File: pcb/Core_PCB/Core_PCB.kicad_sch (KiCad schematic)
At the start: 0 parts

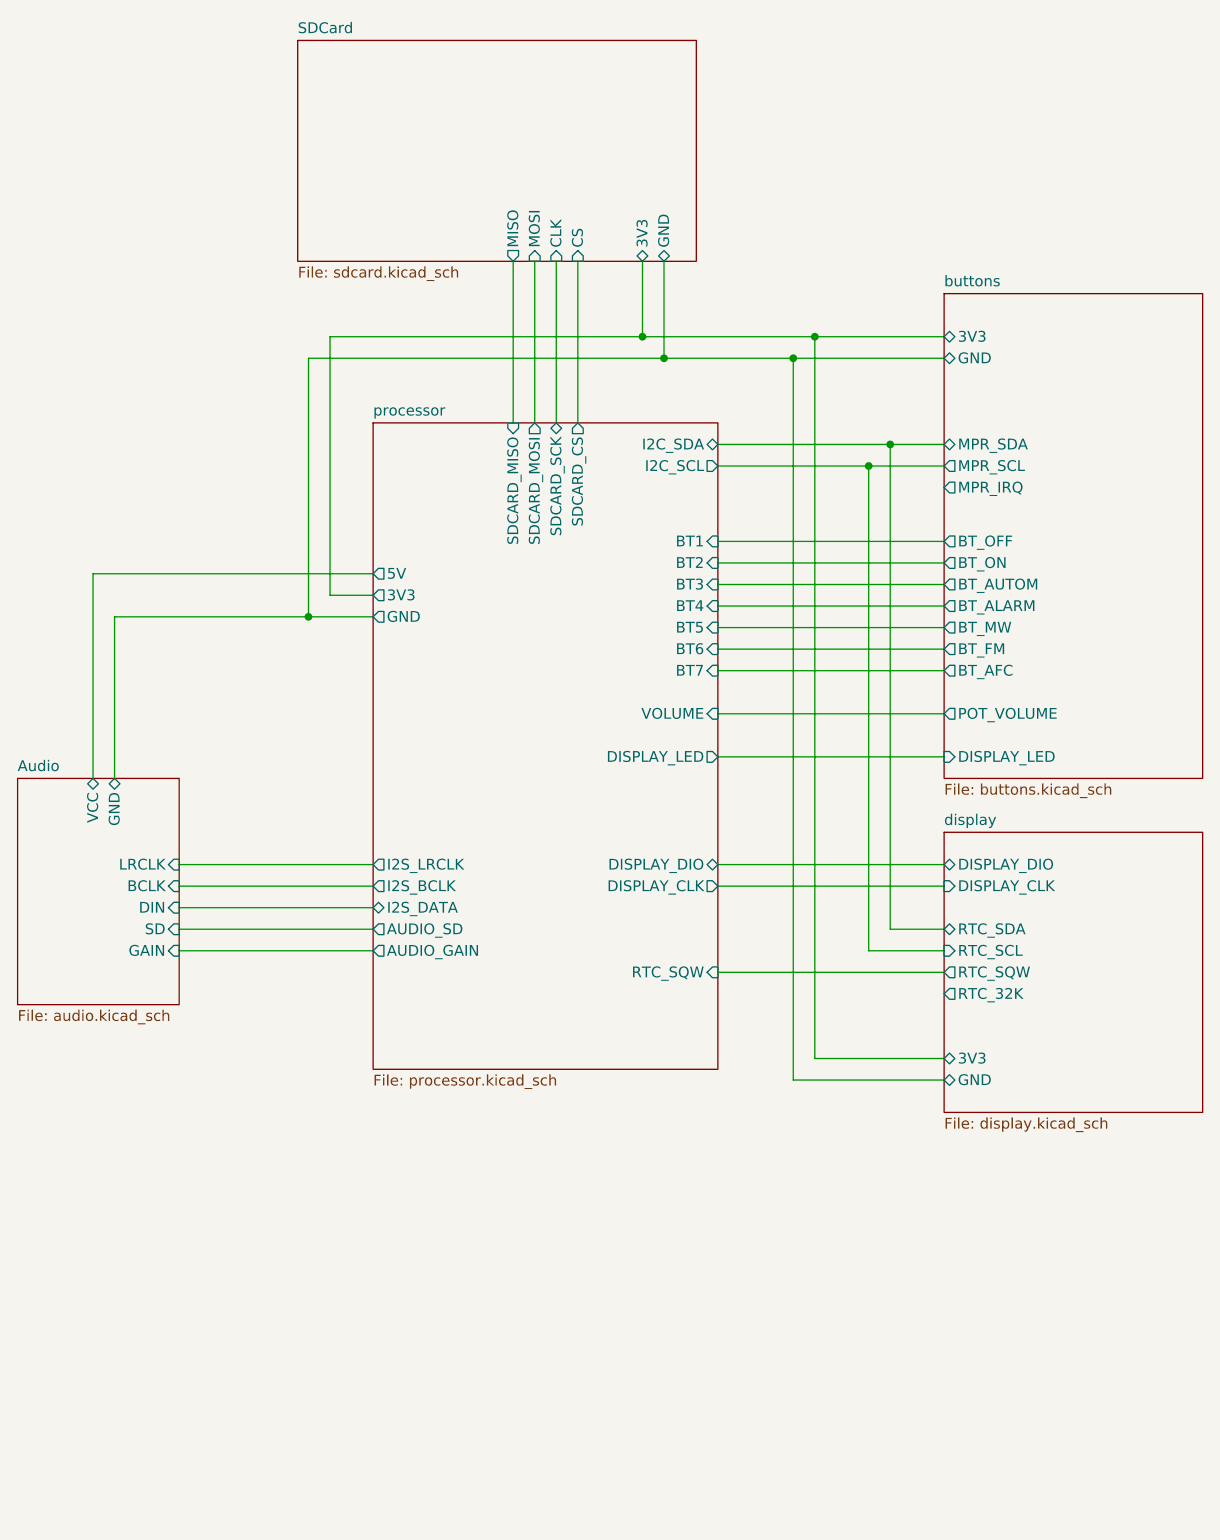
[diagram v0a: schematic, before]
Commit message: SCH: audio gain control via mux (HEF4051), buttons read via i2c io expander (MCP23017)
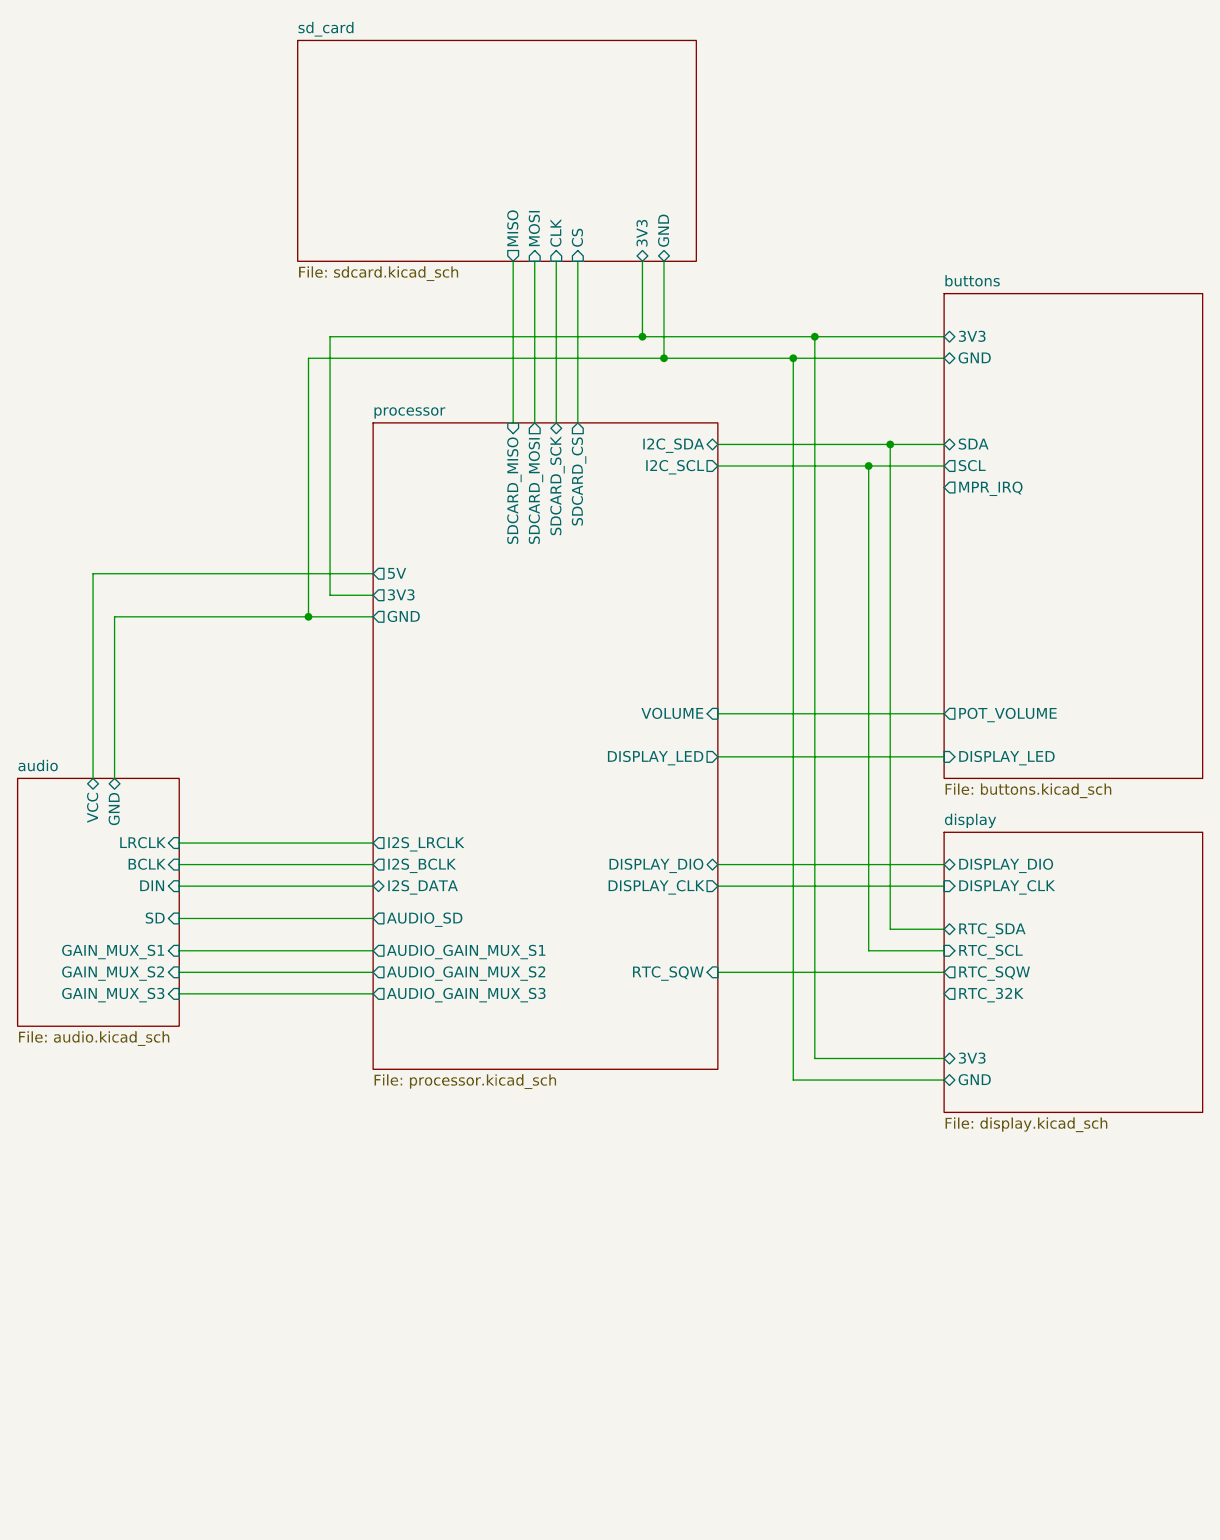
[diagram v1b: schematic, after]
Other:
- sheet Audio renamed audio
- sheet SDCard renamed sd_card
- sheet audio ports: added GAIN_MUX_S1, GAIN_MUX_S2, GAIN_MUX_S3; removed GAIN
- sheet buttons ports: added SCL, SDA; removed BT_AFC, BT_ALARM, BT_AUTOM, BT_FM, BT_MW, BT_OFF, BT_ON, MPR_SCL, MPR_SDA
- sheet processor ports: added AUDIO_GAIN_MUX_S1, AUDIO_GAIN_MUX_S2, AUDIO_GAIN_MUX_S3; removed AUDIO_GAIN, BT1, BT2, BT3, BT4, BT5, BT6, BT7

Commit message: SCH: annotated sheets, reannotated all components
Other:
- company: (none) -> brunolalb@gmail.com
- title: (none) -> Alarm Clock Resto Mod - Core PCB
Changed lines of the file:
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@@
 	(generator_version "10.0")
 	(paper "A4")
+	(title_block
+		(title "Alarm Clock Resto Mod - Core PCB")
+		(date "2026-07-08")
+		(rev "1.0")
+		(company "brunolalb@gmail.com")
+		(comment 1 "Bruno Landau Albrecht")
+	)
 	(junction
 		(at 135.89 53.34)
@@
 			(project "Core_PCB"
 				(path "/79975d02-cfea-4cc3-8869-9743c86248b2"
-					(page "2")
+					(page "3")
 				)
 			)
@@
 			(project "Core_PCB"
 				(path "/79975d02-cfea-4cc3-8869-9743c86248b2"
-					(page "3")
-				)
-			)
+					(page "2")
+				)
+			)

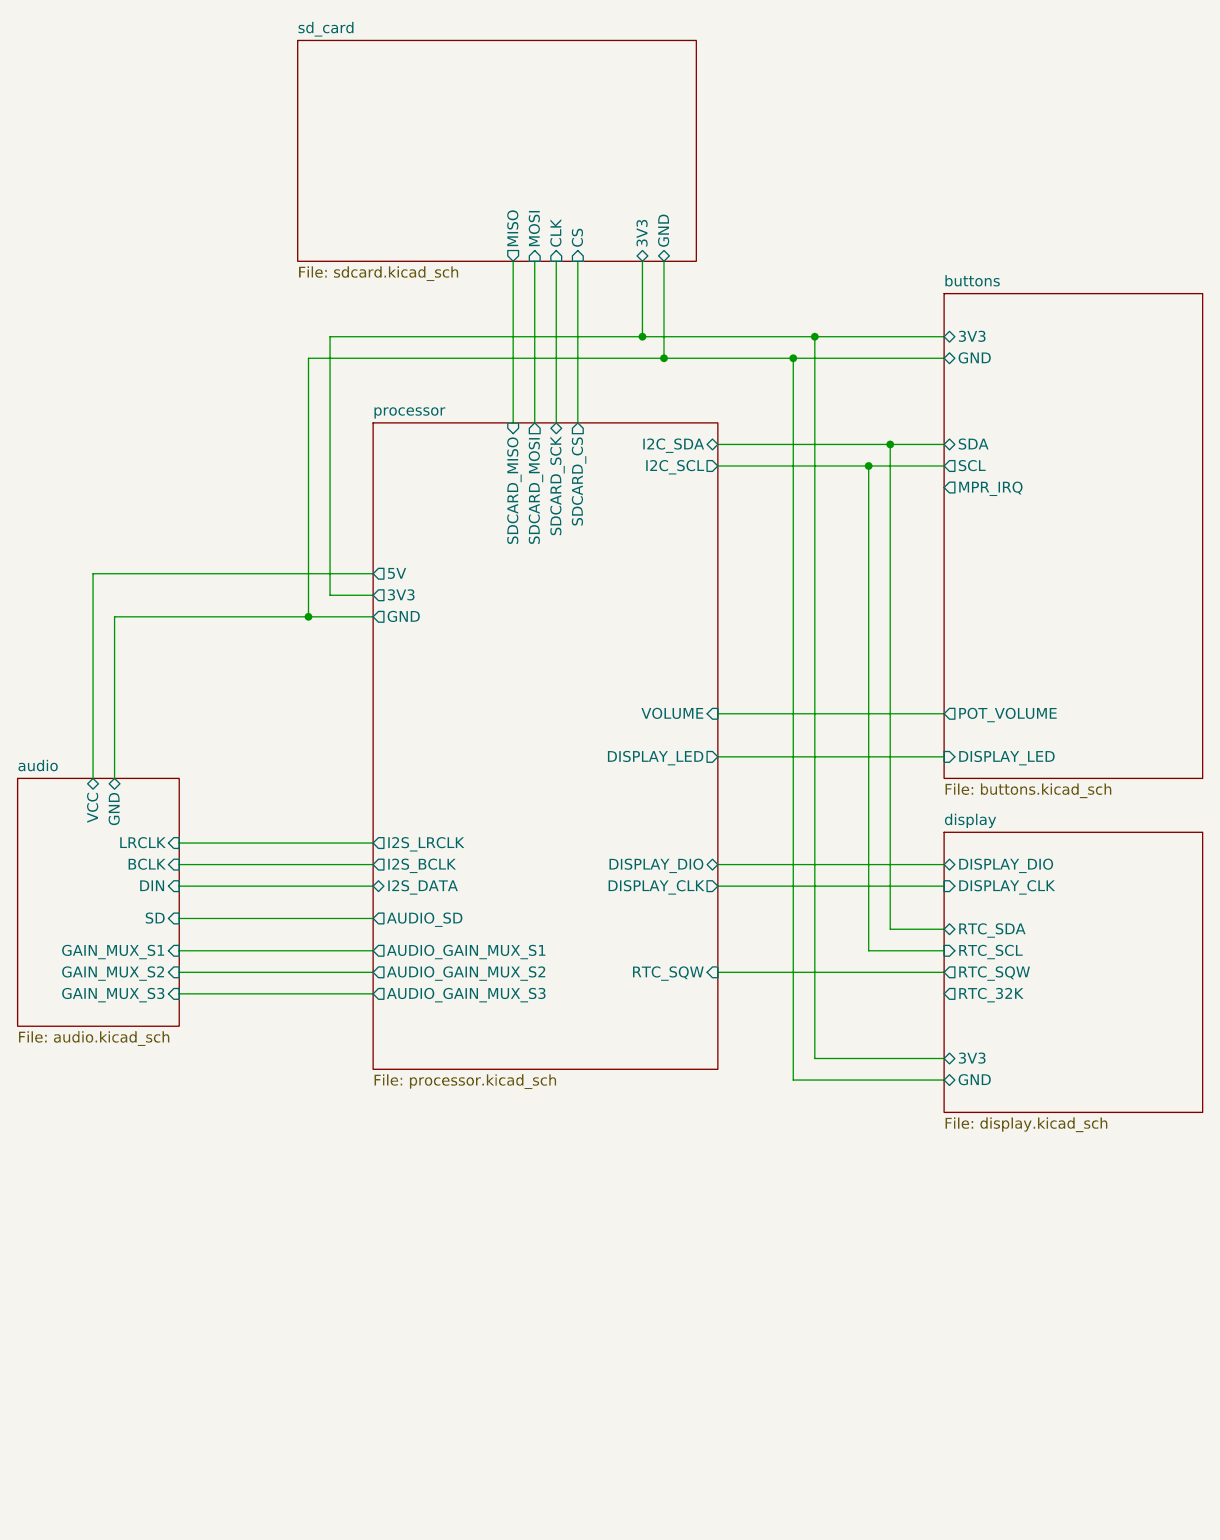
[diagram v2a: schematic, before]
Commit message: SCH: assigned footprints to what had missing, replaced some polarized caps with non polarized, added connector for capacitance sensor, ran electric test and fixed minor issues
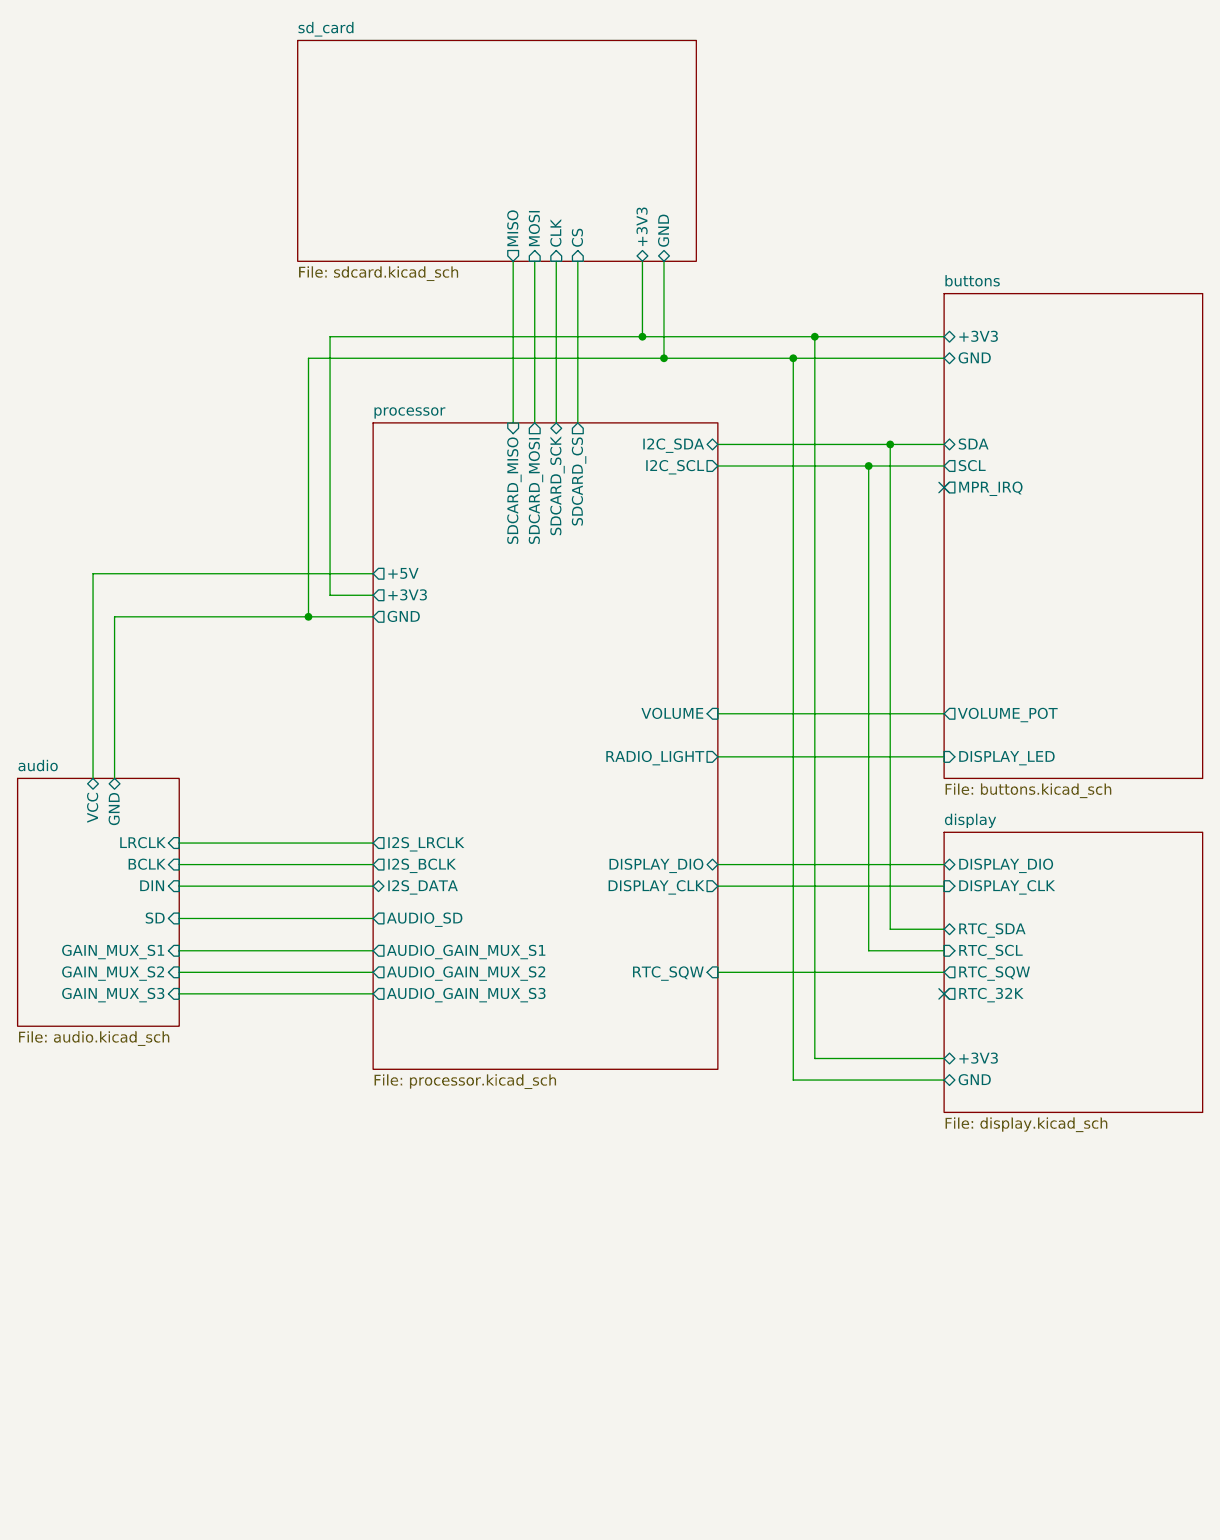
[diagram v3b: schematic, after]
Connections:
- no-connect marks 0 -> 2
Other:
- sheet buttons ports: added +3V3, VOLUME_POT; removed 3V3, POT_VOLUME
- sheet display ports: added +3V3; removed 3V3
- sheet processor ports: added +3V3, +5V, RADIO_LIGHT; removed 3V3, 5V, DISPLAY_LED
- sheet sd_card ports: added +3V3; removed 3V3
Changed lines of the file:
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@@
 		(color 0 0 0 0)
+	)
+	(no_connect
+		(at 171.45 130.81)
+	)
+	(no_connect
+		(at 171.45 71.12)
 	)
 	(wire
@@
 			)
 		)
-		(pin "3V3" bidirectional
+		(pin "+3V3" bidirectional
 			(at 171.45 138.43 180)
 			(effects
@@
 			)
 		)
-		(pin "POT_VOLUME" output
-			(at 171.45 97.79 180)
-			(effects
-				(font
-					(size 1.27 1.27)
-				)
-				(justify left)
-			)
-		)
 		(pin "GND" bidirectional
 			(at 171.45 55.88 180)
@@
 			)
 		)
-		(pin "3V3" bidirectional
-			(at 171.45 53.34 180)
-			(effects
-				(font
-					(size 1.27 1.27)
-				)
-				(justify left)
-			)
-		)
 		(pin "MPR_IRQ" output
 			(at 171.45 71.12 180)
@@
 		(pin "SCL" output
 			(at 171.45 68.58 180)
+			(effects
+				(font
+					(size 1.27 1.27)
+				)
+				(justify left)
+			)
+		)
+		(pin "+3V3" bidirectional
+			(at 171.45 53.34 180)
+			(effects
+				(font
+					(size 1.27 1.27)
+				)
+				(justify left)
+			)
+		)
+		(pin "VOLUME_POT" output
+			(at 171.45 97.79 180)
 			(effects
 				(font
@@
 			)
 		)
-		(pin "3V3" bidirectional
-			(at 135.89 44.45 270)
-			(effects
-				(font
-					(size 1.27 1.27)
-				)
-				(justify left)
-			)
-		)
 		(pin "MISO" output
 			(at 120.65 44.45 270)
@@
 		(pin "CLK" input
 			(at 125.73 44.45 270)
+			(effects
+				(font
+					(size 1.27 1.27)
+				)
+				(justify left)
+			)
+		)
+		(pin "+3V3" bidirectional
+			(at 135.89 44.45 270)
 			(effects
 				(font
@@
 			)
 		)
-		(pin "3V3" output
-			(at 104.14 83.82 180)
-			(effects
-				(font
-					(size 1.27 1.27)
-				)
-				(justify left)
-			)
-		)
-		(pin "5V" output
-			(at 104.14 81.28 180)
-			(effects
-				(font
-					(size 1.27 1.27)
-				)
-				(justify left)
-			)
-		)
 		(pin "GND" output
 			(at 104.14 86.36 180)
@@
 			)
 		)
-		(pin "DISPLAY_LED" output
-			(at 144.78 102.87 0)
-			(effects
-				(font
-					(size 1.27 1.27)
-				)
-				(justify right)
-			)
-		)
 		(pin "AUDIO_GAIN_MUX_S2" output
 			(at 104.14 128.27 180)
@@
 			)
 		)
+		(pin "+3V3" output
+			(at 104.14 83.82 180)
+			(effects
+				(font
+					(size 1.27 1.27)
+				)
+				(justify left)
+			)
+		)
+		(pin "+5V" output
+			(at 104.14 81.28 180)
+			(effects
+				(font
+					(size 1.27 1.27)
+				)
+				(justify left)
+			)
+		)
+		(pin "RADIO_LIGHT" output
+			(at 144.78 102.87 0)
+			(effects
+				(font
+					(size 1.27 1.27)
+				)
+				(justify right)
+			)
+		)
